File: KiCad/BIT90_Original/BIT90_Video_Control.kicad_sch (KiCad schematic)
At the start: 26 parts, among them U10 74LS04, U15 74LS107, U16 TMS9929A, U17 MK4116N, U18 MK4116N, U19 MK4116N, U20 MK4116N, U21 MK4116N, U22 MK4116N, U23 MK4116N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

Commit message: Added "Joystick, Audio, Tape Out" schematic
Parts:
- C11: renamed from C??; value ~ -> 100nF (104)
- C8: renamed from C??; value ?? -> 100nF (104)
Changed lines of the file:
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@@
 		(comment 4 "Based on original schematics from BIT Corporation")
 	)
-	(text_box "Looks like \"C12\" but this is assigned already"
+	(text_box "Marked as \"C12\" on original schematic"
 		(exclude_from_sim no)
 		(at 260.35 59.69 0)
-		(size 12.7 11.43)
+		(size 12.7 10.16)
 		(margins 0.9525 0.9525 0.9525 0.9525)
 		(stroke
@@
 	(text_box "Unmarked on original schematic"
 		(exclude_from_sim no)
-		(at 162.56 148.59 0)
+		(at 163.83 153.67 0)
 		(size 12.7 7.62)
 		(margins 0.9525 0.9525 0.9525 0.9525)
@@
 		)
 	)
+	(wire
+		(pts
+			(xy 182.88 104.14) (xy 182.88 120.65)
+		)
+		(stroke
+			(width 0)
+			(type default)
+		)
+	)
 	(bus
 		(pts
@@
 	(wire
 		(pts
+			(xy 182.88 133.35) (xy 182.88 120.65)
+		)
+		(stroke
+			(width 0)
+			(type default)
+		)
+	)
+	(wire
+		(pts
 			(xy 113.03 88.9) (xy 124.46 88.9)
 		)
@@
 	(wire
 		(pts
-			(xy 182.88 104.14) (xy 182.88 120.65)
-		)
-		(stroke
-			(width 0)
-			(type default)
-		)
-	)
-	(wire
-		(pts
 			(xy 113.03 127) (xy 124.46 127)
 		)
@@
 	(wire
 		(pts
-			(xy 182.88 120.65) (xy 182.88 133.35)
-		)
-		(stroke
-			(width 0)
-			(type default)
-		)
-	)
-	(wire
-		(pts
 			(xy 255.27 115.57) (xy 255.27 124.46)
 		)
@@
 	)
 	(label "VDPΦ"
-		(at 182.88 119.38 0)
+		(at 182.88 133.35 0)
 		(effects
 			(font
@@
 		(dnp no)
 		(fields_autoplaced yes)
-		(property "Reference" "C??"
-			(at 257.81 55.8799 0)
+		(property "Reference" "C11"
+			(at 257.81 54.6099 0)
 			(effects
 				(font
@@
 			)
 		)
-		(property "Value" "~"
+		(property "Value" "100nF (104)"
 			(at 257.81 57.1499 0)
 			(effects
@@
 			(project "BIT90_Original"
 				(path "/d65498c3-6385-4920-ac0f-4c76daf90780/e454d622-f3e6-467f-ab52-84d3deb6b624"
-					(reference "C??")
+					(reference "C11")
 					(unit 1)
 				)
@@
 		(on_board yes)
 		(dnp no)
-		(property "Reference" "C??"
-			(at 177.8 148.59 0)
+		(property "Reference" "C8"
+			(at 177.8 148.336 0)
 			(effects
 				(font
@@
 			)
 		)
-		(property "Value" "??"
-			(at 177.8 150.622 0)
+		(property "Value" "100nF (104)"
+			(at 173.228 150.622 0)
 			(effects
 				(font
@@
 			(project "BIT90_Original"
 				(path "/d65498c3-6385-4920-ac0f-4c76daf90780/e454d622-f3e6-467f-ab52-84d3deb6b624"
-					(reference "C??")
+					(reference "C8")
 					(unit 1)
 				)

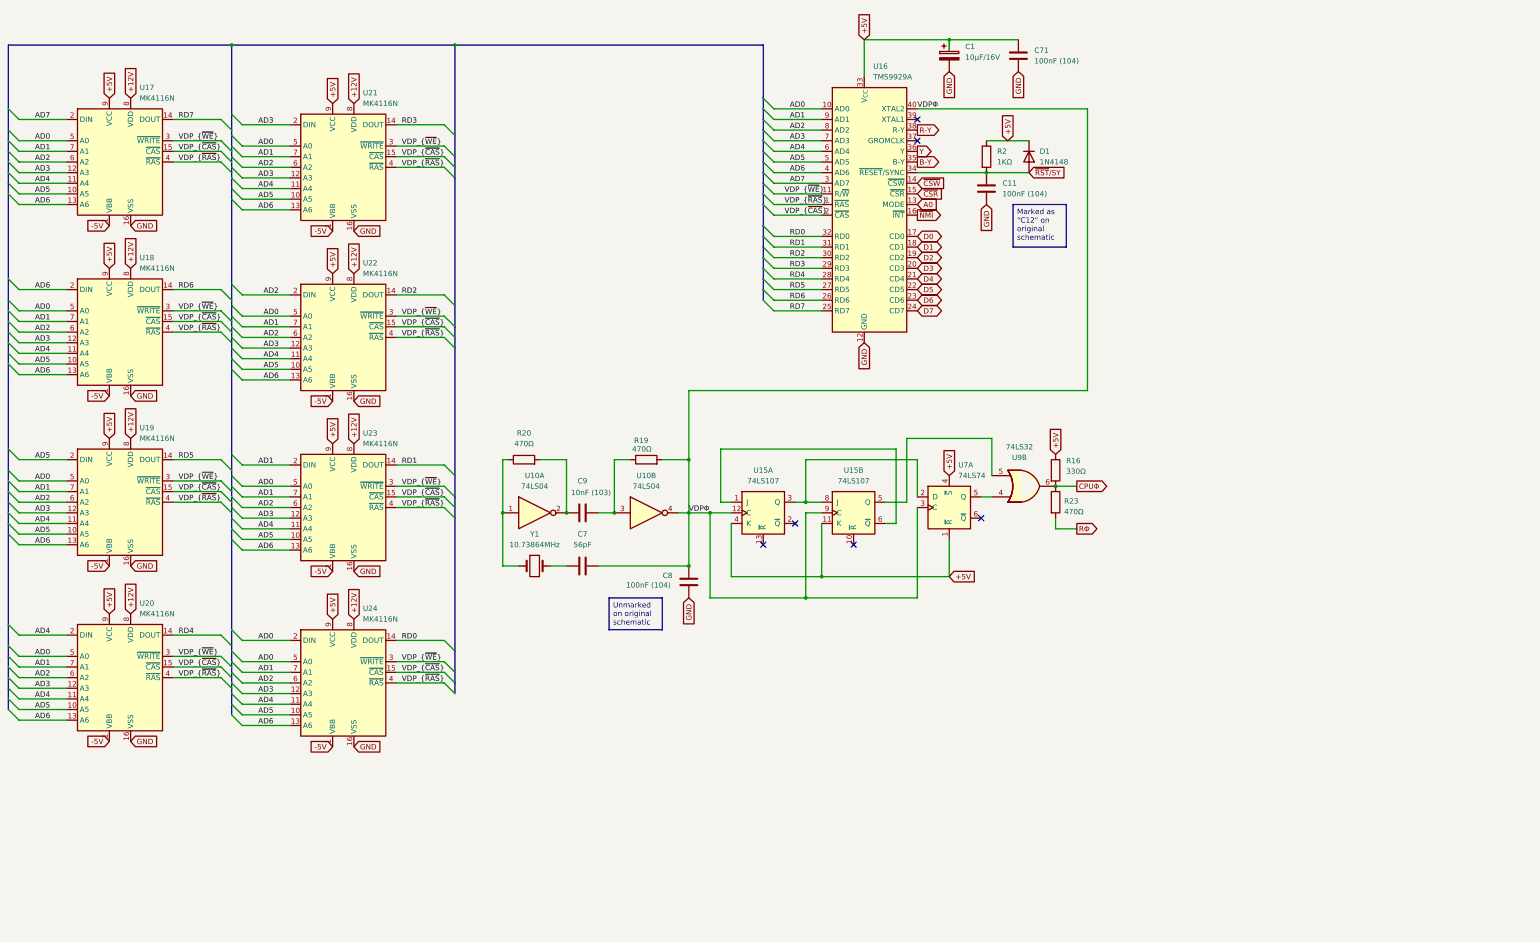
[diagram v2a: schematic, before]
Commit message: Completed original schematic redraw
Well, didn't finish the Video Encoder (PAL) sheet as I'm not going to use any of it in the new design.
Moved the audio output from that sheet to the Joystick/Audio/Tape out sheet where the sound generator is.
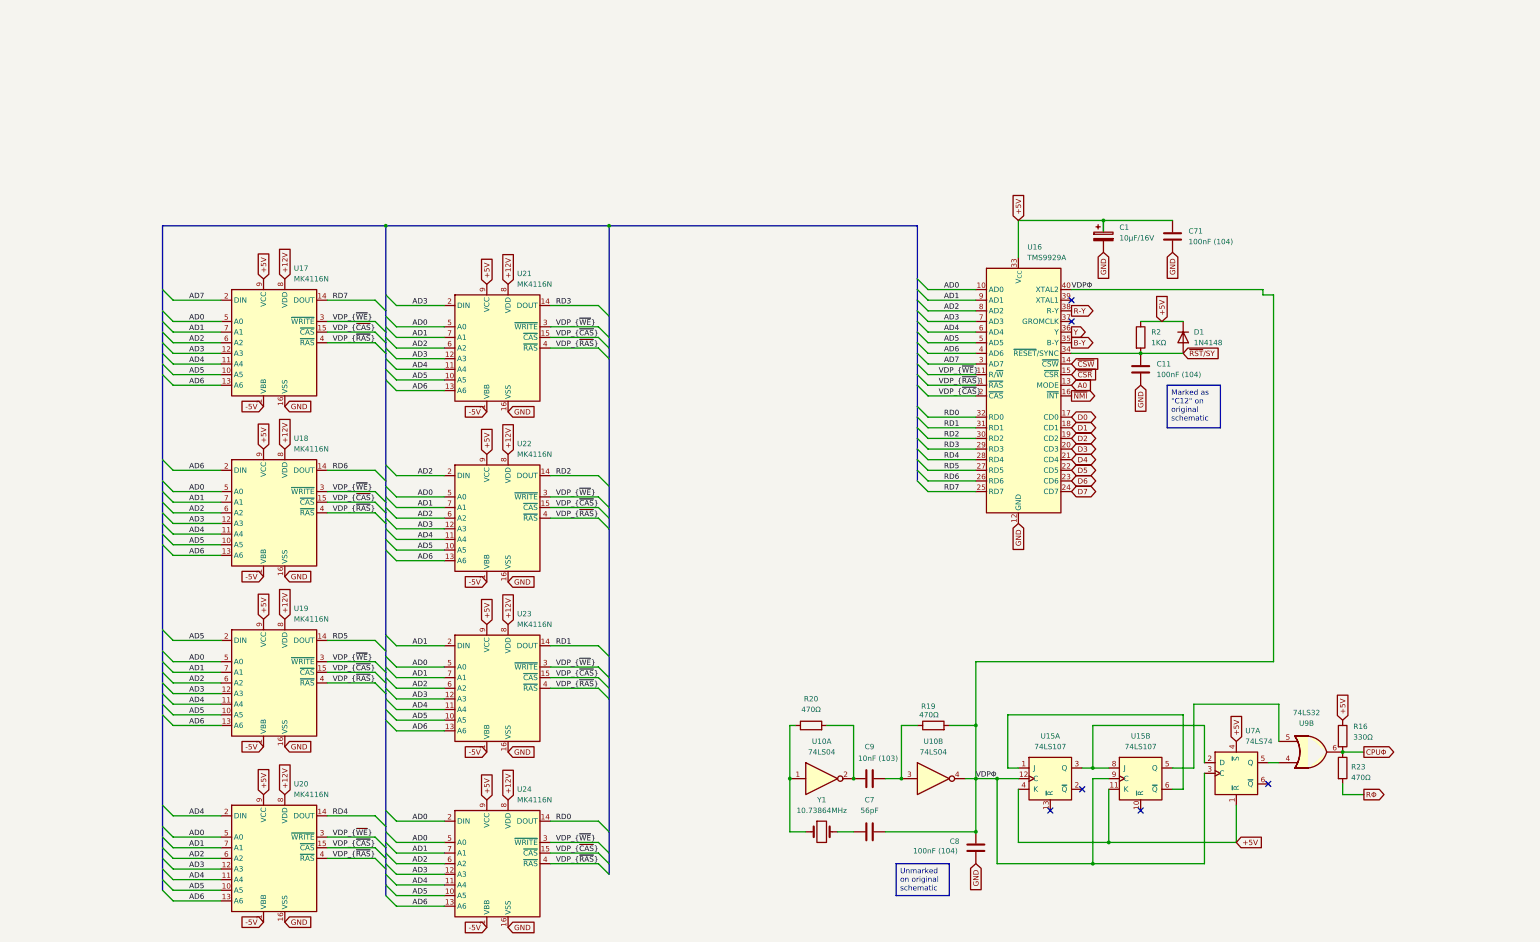
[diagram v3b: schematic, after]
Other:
- moved on the sheet: C1, C11, C7, C71, C8, C9, D1, R16, R19, R2, R20, R23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

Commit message: Small updates/corrections
Managed to figure out some more errors/missing info from ColecoVision schematics & Henk's BIT90 motherboard underside photo
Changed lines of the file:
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@@
 	(title_block
 		(title "BIT90 Video Control (PAL)")
-		(date "3/JUN/2026")
+		(date "5/JUN/2026")
 		(rev "A")
 		(company "Brett Hallen")
@@
 		(margins 0.9525 0.9525 0.9525 0.9525)
 		(stroke
+			(width 0)
+			(type solid)
+		)
+		(fill
+			(type none)
+		)
+		(effects
+			(font
+				(size 1.27 1.27)
+			)
+			(justify left top)
+		)
+	)
+	(text_box "CPUΦ = CPU clock\nVDPΦ = video clock\nRΦ = current-limited CPU clock to expansion\nEXTΦ = audio clock but from where?"
+		(exclude_from_sim no)
+		(at 328.93 207.01 0)
+		(size 50.8 10.16)
+		(margins 0.9525 0.9525 0.9525 0.9525)
+		(stroke

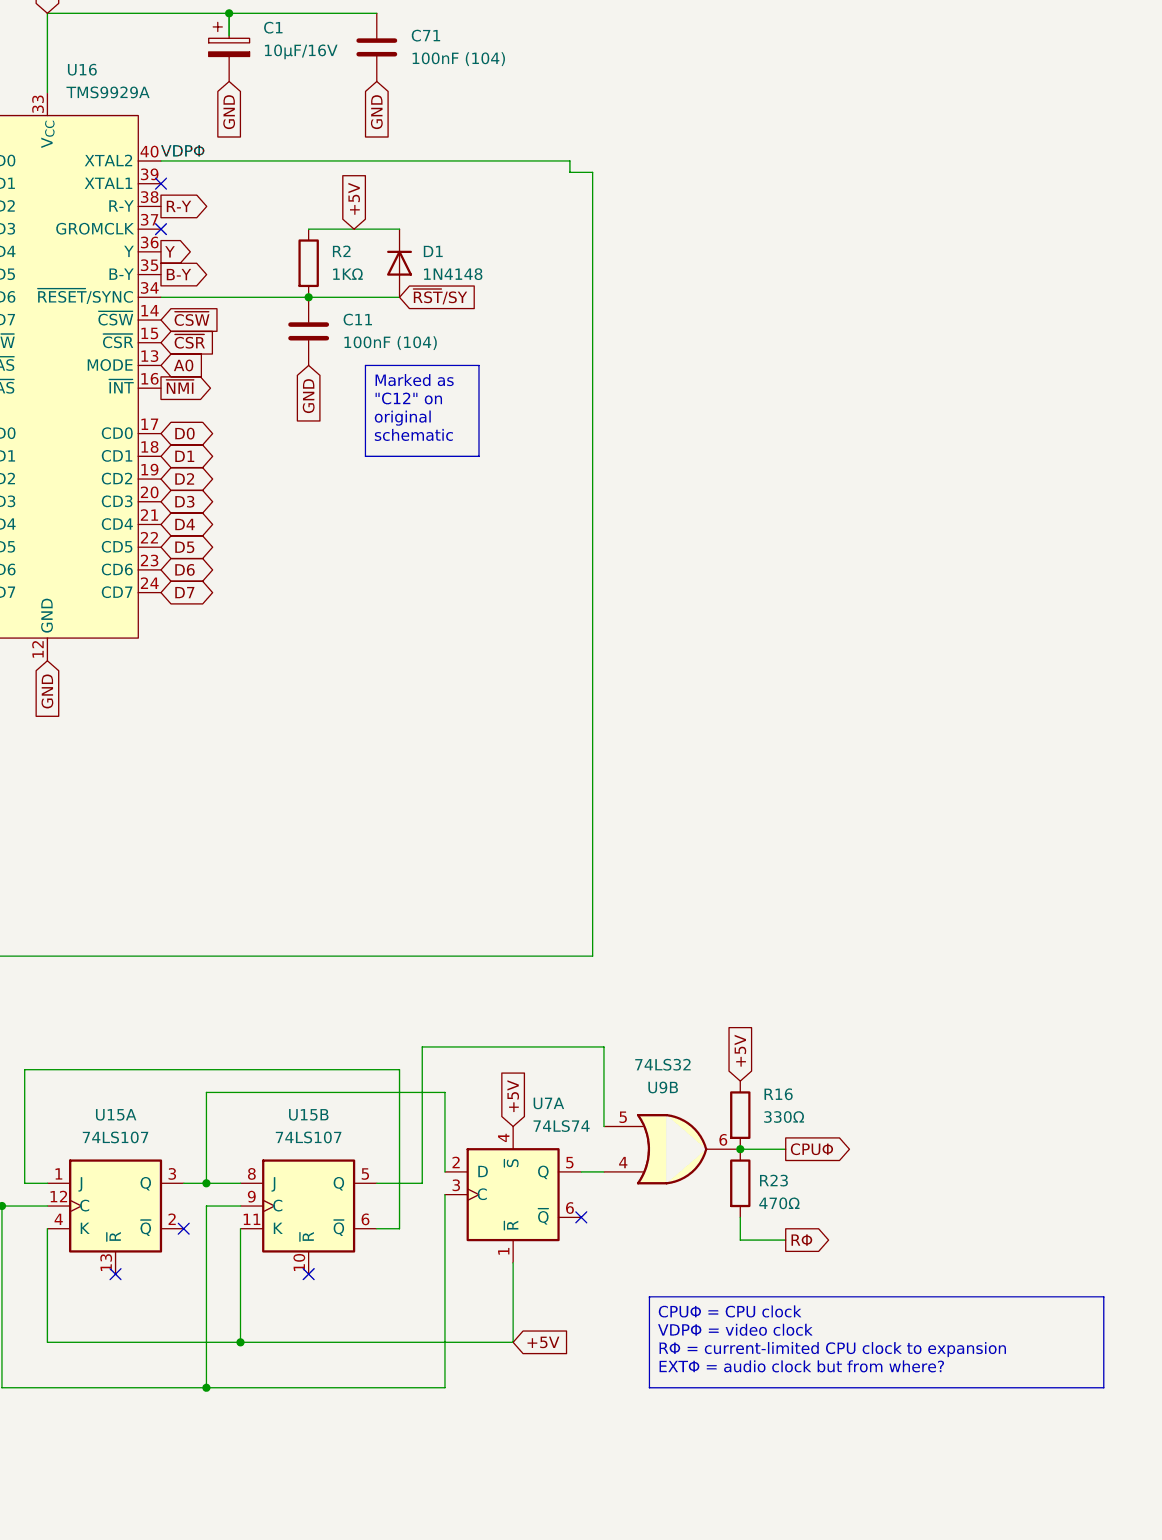
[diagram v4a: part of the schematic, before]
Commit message: Resolved audio clock signal
Marked as EXTΦ on BIT90 schematic, generated via resistor from CPUΦ
Renamed it as AUDΦ so it's a bit clearer
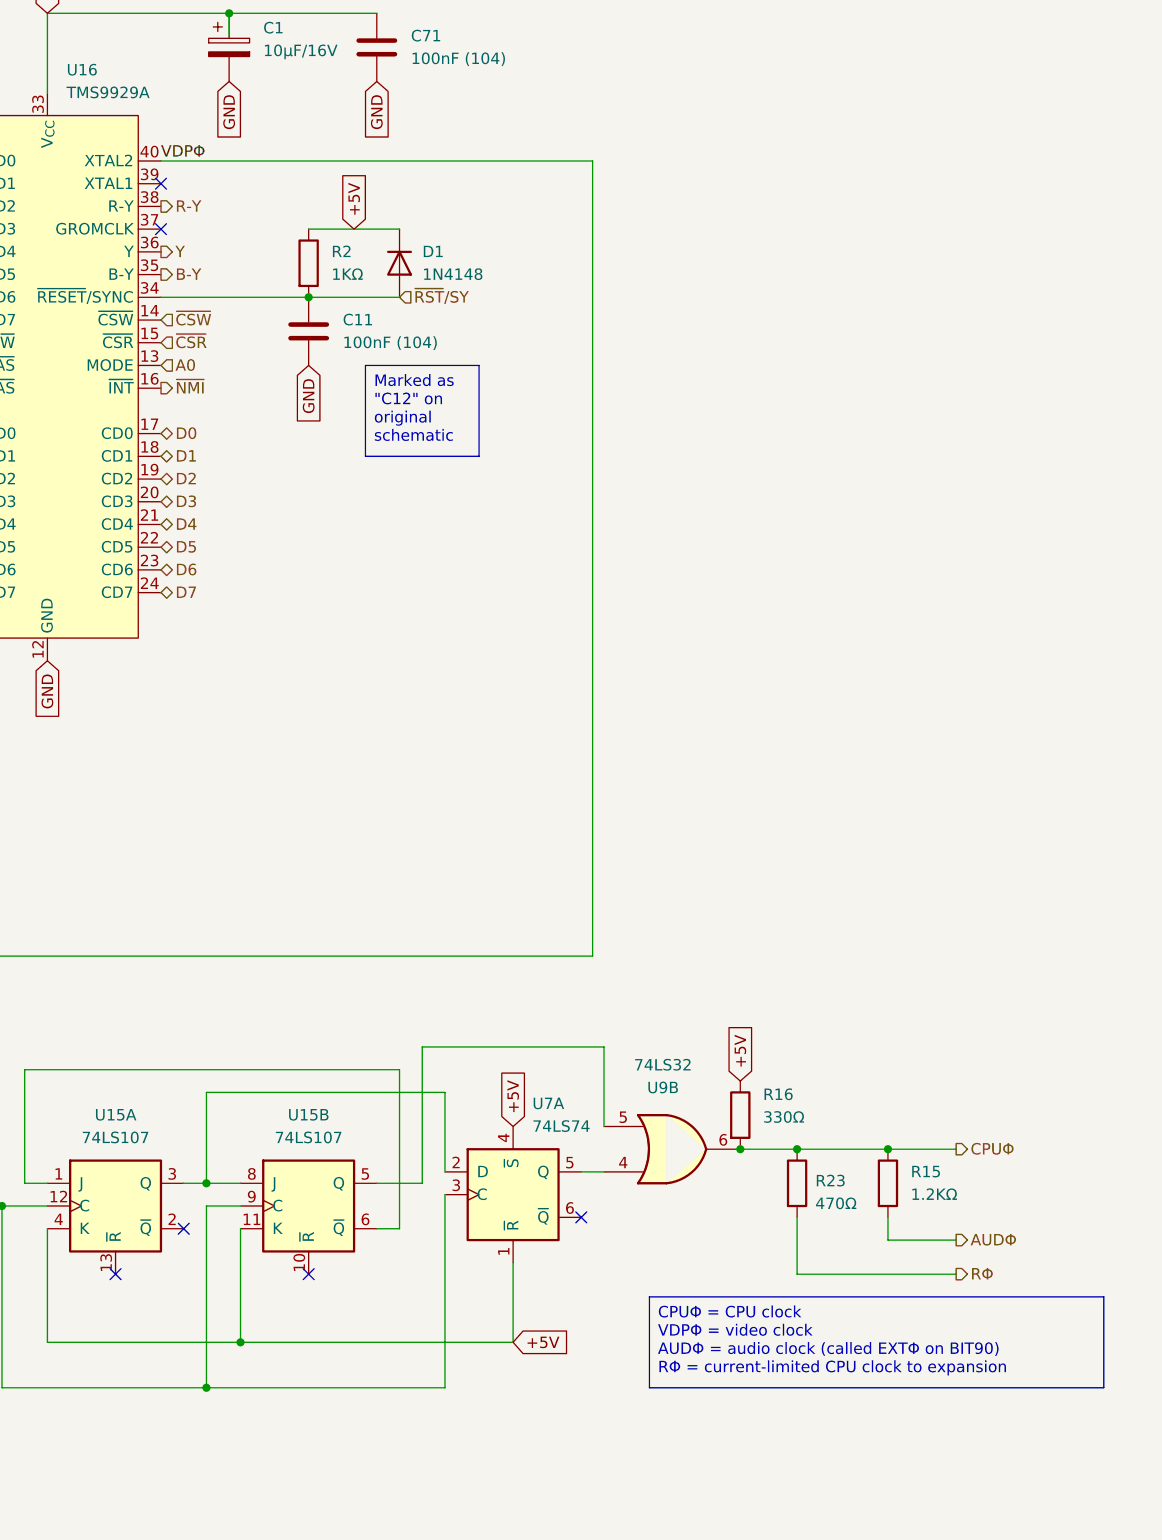
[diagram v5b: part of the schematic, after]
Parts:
- added R15: 1.2KΩ, symbol Device:R
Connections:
- net CPUΦ: now also R15.1
- new net AUDΦ: R15.2
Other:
- moved on the sheet: R23
